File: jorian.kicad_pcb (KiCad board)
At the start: 2 copper layers, 98.9 x 100 mm, 90 parts, among them J6 lipo_charger, U3 LP3990-3.3v

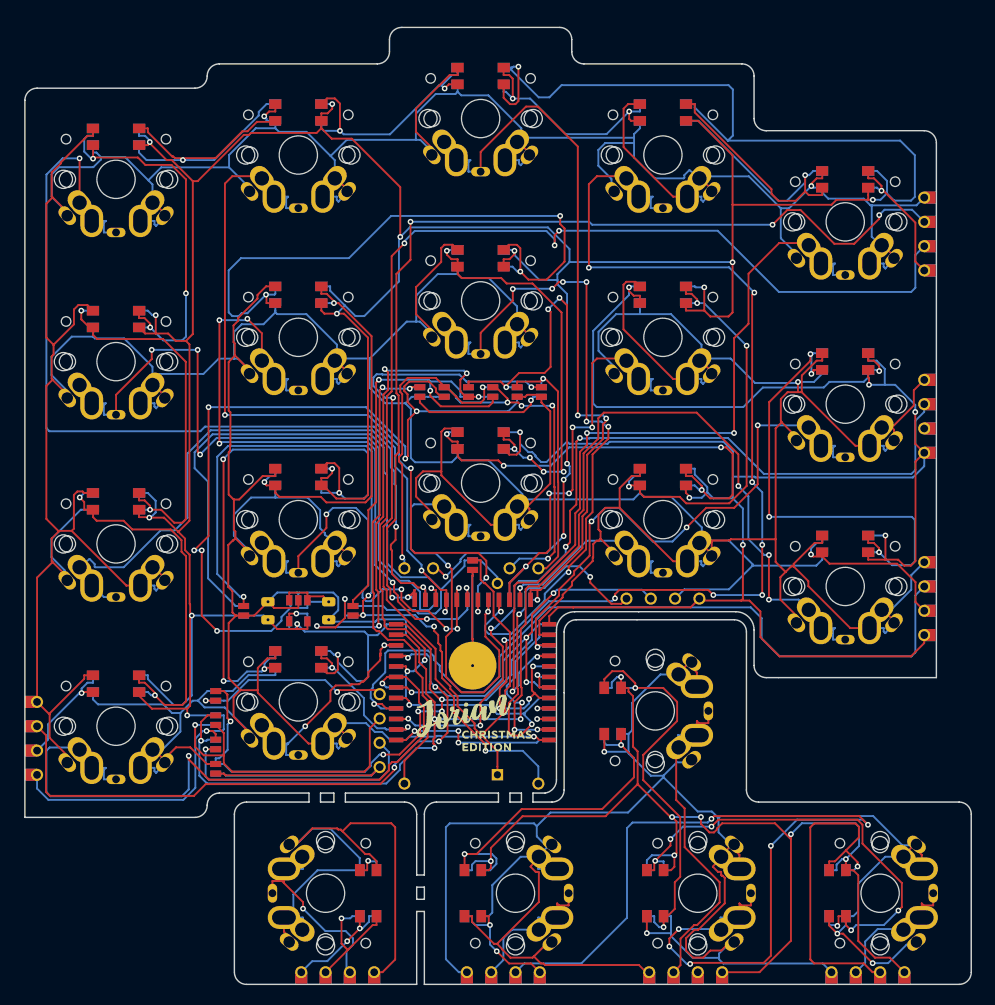
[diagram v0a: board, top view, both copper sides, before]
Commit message: Ready for 0.15 (6 mil) tolerances
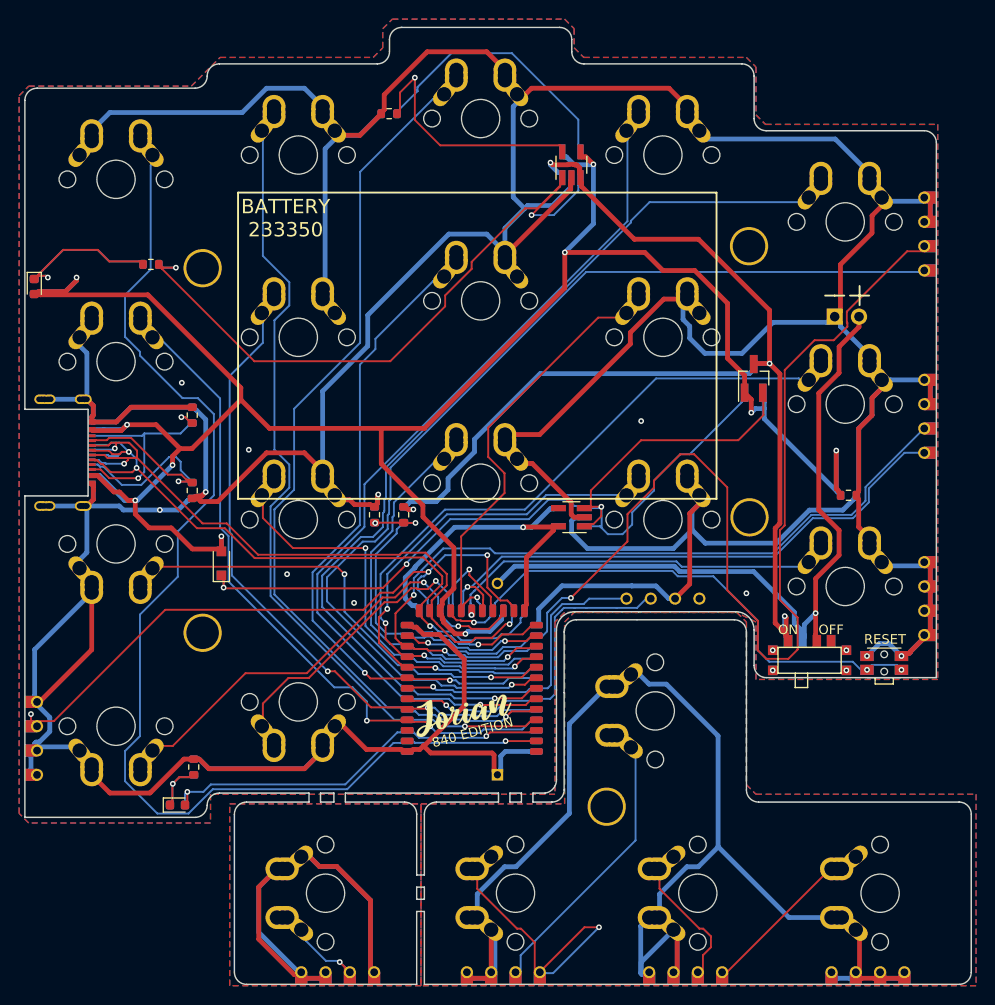
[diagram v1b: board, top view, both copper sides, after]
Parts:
- removed C1, C2: 1uF, kbd:C_0805
- removed H1: Battery Pad, kbd:battery_pad
- removed J6: lipo_charger, kbd:lipo_charger_03962A
- removed JP1: +, kbd:jumper
- removed JP10: -, kbd:jumper
- removed JP11, JP22: VUSB, kbd:jumper
- removed JP12, JP23: GND, kbd:jumper
- removed JP13, JP24: OUT+, kbd:jumper
- removed JP14, JP18, JP25: LIPO+, kbd:jumper
- removed JP15, JP19, JP26: LIPO-, kbd:jumper
- removed JP17, JP27: OUT-, kbd:jumper
- removed JP2, JP3, JP4, JP5, JP6, JP7, JP8, JP9: , kbd:jumper
- removed JP20: BAT+, kbd:jumper
- removed JP21: BAT-, kbd:jumper
- removed L1, L10, L11, L12, L13, L14, L15, L16, L17, L18, L19, L2, L20, L21, L22, L3, L4, L5, L6, L7, L8, L9: SK6812MINI, kbd:kbd_SK6812MINI
- removed OLED1: I2C_conn, kbd:connector_i2c
- added D1: RED, skean:LED_0603_1608Metric_REV, F.Cu at (42.3, 65.8)
- added D2: 1N5819, skean:D_SOD-323_HandSoldering_REV, F.Cu at (61.8, 94.7)
- added D3: BLUE, skean:LED_0603_1608Metric_REV, F.Cu at (57.2, 120.0)
- added HM1: CaseHole, kbd:M2-MountingHole-Standoff, F.Cu at (59.9, 63.9)
- added HM2: CaseHole, kbd:M2-MountingHole-Standoff, F.Cu at (117.0, 61.6)
- added HM3: CaseHole, kbd:M2-MountingHole-Standoff, F.Cu at (59.9, 102.0)
- added HM4: CaseHole, kbd:M2-MountingHole-Standoff, F.Cu at (117.0, 89.9)
- added HM5: CaseHole, kbd:M2-MountingHole-Standoff, F.Cu at (102.1, 120.2)
- added J1: USB-C Conn, skean:USB-C_C168688_REV, F.Cu at (41.3, 83.2)
- added J2: Ex_Bat, skean:Battery_TH, F.Cu at (125.9, 69.0)
- added Q1: AO3407, skean:SOT-23_Handsoldering_REV, F.Cu at (117.4, 75.4)
- added R1: 5.1K, skean:R_0603_1608Metric_REV, F.Cu at (58.8, 79.2)
- added R2: 5.1K, skean:R_0603_1608Metric_REV, F.Cu at (58.8, 87.1)
- added R3: 1K, skean:R_0603_1608Metric_REV, F.Cu at (54.4, 63.5)
- added R4: RPROG, skean:R_0603_1608Metric_REV, F.Cu at (79.3, 47.8)
- added R5: 820K, skean:R_0603_1608Metric_REV, F.Cu at (80.9, 89.7)
- added R6: 2M, skean:R_0603_1608Metric_REV, F.Cu at (77.8, 89.7)
- added R7: 100K, skean:R_0603_1608Metric_REV, F.Cu at (127.3, 87.6)
- added R8: 1K, skean:R_0603_1608Metric_REV, F.Cu at (58.9, 116.0)
- added RSW1: SW_PUSH, skean:SW_SPST_EVQP7C_REV, F.Cu at (131.1, 105.1)
- added SW23: SW_SPDT, skean:SW_SPDT+H-MSK12C01_hor(7pin_SMD)_REV, F.Cu at (123.3, 104.9)
- SW1: renamed from S1; value CHERRY MX -> SW_PUSH; footprint kbd:cherry -> kbd:MX-Alps-1U-REV
- SW10: renamed from S10; value CHERRY MX -> SW_PUSH; footprint kbd:cherry -> kbd:MX-Alps-1U-REV
- SW11: renamed from S11; value CHERRY MX -> SW_PUSH; footprint kbd:cherry -> kbd:MX-Alps-1U-REV
- SW12: renamed from S12; value CHERRY MX -> SW_PUSH; footprint kbd:cherry -> kbd:MX-Alps-1U-REV
- SW13: renamed from S13; value CHERRY MX -> SW_PUSH; footprint kbd:cherry -> kbd:MX-Alps-1U-REV
- SW14: renamed from S14; value CHERRY MX -> SW_PUSH; footprint kbd:cherry -> kbd:MX-Alps-1U-REV
- SW15: renamed from S15; value CHERRY MX -> SW_PUSH; footprint kbd:cherry -> kbd:MX-Alps-1U-REV
- SW16: renamed from S16; value CHERRY MX -> SW_PUSH; footprint kbd:cherry -> kbd:MX-Alps-1U-REV
- SW17: renamed from S17; value CHERRY MX -> SW_PUSH; footprint kbd:cherry -> kbd:MX-Alps-1U-REV
- SW18: renamed from S18; value CHERRY MX -> SW_PUSH; footprint kbd:cherry -> kbd:MX-Alps-1U-REV
- SW19: renamed from S19; value CHERRY MX -> SW_PUSH; footprint kbd:cherry -> kbd:MX-Alps-1U-REV
- SW2: renamed from S2; value CHERRY MX -> SW_PUSH; footprint kbd:cherry -> kbd:MX-Alps-1U-REV
- SW20: renamed from S20; value CHERRY MX -> SW_PUSH; footprint kbd:cherry -> kbd:MX-Alps-1U-REV
- SW21: renamed from S21; value CHERRY MX -> SW_PUSH; footprint kbd:cherry -> kbd:MX-Alps-1U-REV
- SW22: renamed from S22; value CHERRY MX -> SW_PUSH; footprint kbd:cherry -> kbd:MX-Alps-1U-REV
- SW3: renamed from S3; value CHERRY MX -> SW_PUSH; footprint kbd:cherry -> kbd:MX-Alps-1U-REV
- SW4: renamed from S4; value CHERRY MX -> SW_PUSH; footprint kbd:cherry -> kbd:MX-Alps-1U-REV
- SW5: renamed from S5; value CHERRY MX -> SW_PUSH; footprint kbd:cherry -> kbd:MX-Alps-1U-REV
- SW6: renamed from S6; value CHERRY MX -> SW_PUSH; footprint kbd:cherry -> kbd:MX-Alps-1U-REV
- SW7: renamed from S7; value CHERRY MX -> SW_PUSH; footprint kbd:cherry -> kbd:MX-Alps-1U-REV
- SW8: renamed from S8; value CHERRY MX -> SW_PUSH; footprint kbd:cherry -> kbd:MX-Alps-1U-REV
- SW9: renamed from S9; value CHERRY MX -> SW_PUSH; footprint kbd:cherry -> kbd:MX-Alps-1U-REV
- U1: value ~ -> Holyiot-18010; footprint kbd:nrf51822_smd -> kbd:Holyiot-18010-nRF52840-REV
- U2: value ~ -> TP4054; footprint kbd:nrf51822_smd -> skean:SOT-23-5_HandSoldering_REV; moved to F.Cu
- U3: value LP3990-3.3v -> XC6220B331MR-G; footprint kbd:SOT-23-5 -> skean:SOT-23-5_HandSoldering_REV
- moved U2 54.5 mm to (98.4, 53.1), turned to 90 degrees
- moved U3 30.2 mm to (98.4, 89.9), turned to 180 degrees
- moved U1 2.14 mm to (88.0, 108.7), turned to 180 degrees
- turned SW11 to 180 degrees
- turned SW16 to 180 degrees
- turned SW17 to 180 degrees
- turned SW18 to 90 degrees
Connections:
- net OUT+ renamed Net-(D2-Pad1)
- BT1 pad 1: BAT+ -> VBAT
- BT1 pad 2: BAT- -> GND
- E10 pad 2: /S22 -> GND
- E10 pad 3: Net-(E10-Pad3) -> R2C1
- E10 pad 4: VCC -> R3C1
- E15 pad 2: /S21 -> GND
- E15 pad 3: /DIN21 -> GND
- E15 pad 4: VCC -> GND
- E16 pad 2: /S18 -> R4C7
- E16 pad 3: /DIN18 -> GND
- E16 pad 4: VCC -> GND
- E18 pad 1: /GND_A -> GND_A
- E18 pad 2: /S18_A -> R4C7A
- E18 pad 3: /DIN18_A -> GND_A
- E18 pad 4: /VCC_A -> GND_A
- E19 pad 1: /GND_B -> GND_B
- E19 pad 2: /S19_B -> GND_B
- E19 pad 3: /S20_B -> R2C0B
- E19 pad 4: /DIN5_B -> R1C1B
- E20 pad 1: /GND_B -> GND_B
- E20 pad 2: /S22_B -> GND_B
- E20 pad 3: Net-(E20-Pad3) -> R2C1B
- E20 pad 4: /VCC_B -> R3C1B
- E21 pad 1: /GND_B -> GND_B
- E21 pad 2: /S21_B -> GND_B
- E21 pad 3: /DIN21_B -> GND_B
- E21 pad 4: /VCC_B -> GND_B
- E5 pad 2: /S19 -> GND
- E5 pad 3: /S20 -> R2C0
- E5 pad 4: /DIN5 -> R1C1
- SW1 pad 2: /S1 -> R1C6
- SW10 pad 1: GND -> R2C2
- SW10 pad 2: /S10 -> GND
- SW11 pad 1: GND -> R3C6
- SW11 pad 2: /S11 -> GND
- SW12 pad 1: GND -> R3C5
- SW12 pad 2: /S12 -> GND
- SW13 pad 1: GND -> R3C4
- SW13 pad 2: /S13 -> GND
- SW14 pad 1: GND -> R3C3
- SW14 pad 2: /S14 -> GND
- SW15 pad 1: GND -> R3C2
- SW15 pad 2: /S15 -> GND
- SW16 pad 1: GND -> R4C6
- SW16 pad 2: /S16 -> GND
- SW17 pad 2: /S17 -> R4C5
- SW18 pad 1: /GND_A -> R4C7A
- SW18 pad 2: /S18_A -> GND_A
- SW19 pad 1: /GND_B -> GND_B
- SW19 pad 2: /S19_B -> R1C1B
- SW2 pad 1: GND -> R1C5
- SW2 pad 2: /S2 -> GND
- SW20 pad 1: /GND_B -> GND_B
- SW20 pad 2: /S20_B -> R2C1B
- SW21 pad 1: /GND_B -> GND_B
- SW21 pad 2: /S21_B -> R3C1B
- SW22 pad 1: /GND_B -> R2C0B
- SW22 pad 2: /S22_B -> GND_B
- SW3 pad 1: GND -> R1C4
- SW3 pad 2: /S3 -> GND
- SW4 pad 1: GND -> R1C3
- SW4 pad 2: /S4 -> GND
- SW5 pad 1: GND -> R1C2
- SW5 pad 2: /S5 -> GND
- SW6 pad 2: /S6 -> R2C6
- SW7 pad 1: GND -> R2C5
- SW7 pad 2: /S7 -> GND
- SW8 pad 1: GND -> R2C4
- SW8 pad 2: /S8 -> GND
- SW9 pad 1: GND -> R2C3
- SW9 pad 2: /S9 -> GND
- U1 pad 1: GND -> unconnected-(U1-Pad1)
- U1 pad 10: /S10 -> R3C5
- U1 pad 11: GND -> R3C4
- U1 pad 12: VCC -> BATTERY_PIN
- U1 pad 13: /S3 -> PROG
- U1 pad 14: /S14 -> nRF_VDD
- U1 pad 15: /S9 -> R4C7
- U1 pad 16: /S8 -> R4C6
- U1 pad 17: /S13 -> R4C5
- U1 pad 18: /S2 -> R3C1
- U1 pad 19: /S7 -> R3C2
- U1 pad 2: /S15 -> R1C6
- U1 pad 20: /S12 -> R2C3
- U1 pad 21: /S1 -> reset
- U1 pad 22: /S6 -> VBUS
- U1 pad 23: /S11 -> DATA-
- U1 pad 24: /S19 -> DATA+
- U1 pad 25: SDA -> GND
- U1 pad 26: SCL -> R2C0
- U1 pad 27: /S17 -> R2C1
- U1 pad 28: /S18 -> R2C2
- U1 pad 29: /S20 -> R3C3
- U1 pad 3: TX -> BLUE_LED
- U1 pad 30: /S16 -> R2C4
- U1 pad 31: SWD -> SWC
- U1 pad 32: SWC -> SWD
- U1 pad 33: /S21 -> R2C5
- U1 pad 34: /S22 -> R2C6
- U1 pad 35: LED_DATA -> unconnected-(U1-Pad35)
- U1 pad 36: SWO -> unconnected-(U1-Pad36)
- U1 pad 4: /LED -> R1C5
- U1 pad 5: /S4 -> R1C4
- U1 pad 6: RX -> R1C3
- U1 pad 7: Net-(U1-Pad7) -> R1C2
- U1 pad 8: Net-(U1-Pad8) -> R1C1
- U1 pad 9: /S5 -> R3C6
- U2 pad 1: GND -> Net-(R3-Pad2)
- U2 pad 2: LED_DATA -> GND
- U2 pad 3: /S22 -> VBAT2
- U2 pad 4: /S21 -> VBUS
- U2 pad 5: /S20 -> Net-(R4-Pad1)
- U3 pad 4: Net-(U3-Pad4) -> unconnected-(U3-Pad4)
- U3 pad 5: VCC -> nRF_VDD
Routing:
- net VCC: track 635.6 -> 0.00 mm, vias 23 -> 0
- net GND: track 990.4 -> 707.7 mm, vias 4 -> 11
- net /GND_B: track 244.3 -> 0.00 mm, vias 4 -> 0
- net VBUS: track 0.00 -> 244.1 mm, vias 0 -> 10
- net GND_B: track 0.00 -> 147.7 mm
- net R1C6: track 0.00 -> 126.2 mm, vias 0 -> 1
- net VBAT2: track 0.00 -> 124.5 mm, vias 0 -> 4
- net /VCC_B: track 122.5 -> 0.00 mm, vias 7 -> 0
- net R2C0: track 0.00 -> 122.4 mm, vias 0 -> 2
- net /S20: track 120.6 -> 0.00 mm, vias 5 -> 0
- net /S4: track 118.2 -> 0.00 mm, vias 11 -> 0
- net R1C1: track 0.00 -> 107.7 mm, vias 0 -> 1
- net /S19: track 105.7 -> 0.00 mm, vias 5 -> 0
- net R1C2: track 0.00 -> 103.7 mm, vias 0 -> 1
- net /S1: track 100.4 -> 0.00 mm, vias 3 -> 0
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- added copper zone on B.Cu, net GND
- added copper zone on F.Cu, net GND
- added copper zone on B.Cu, net GND_A
- added copper zone on F.Cu, net GND_A
- added copper zone on B.Cu, net GND_B
- added copper zone on F.Cu, net GND_B
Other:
- outline, holes or cut-outs redrawn
- net class Default removed
- board text added: "BATTERY 233350"
